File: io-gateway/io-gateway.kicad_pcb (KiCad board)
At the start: 2 copper layers, 13 parts, among them IC1 MAX17673AATI+

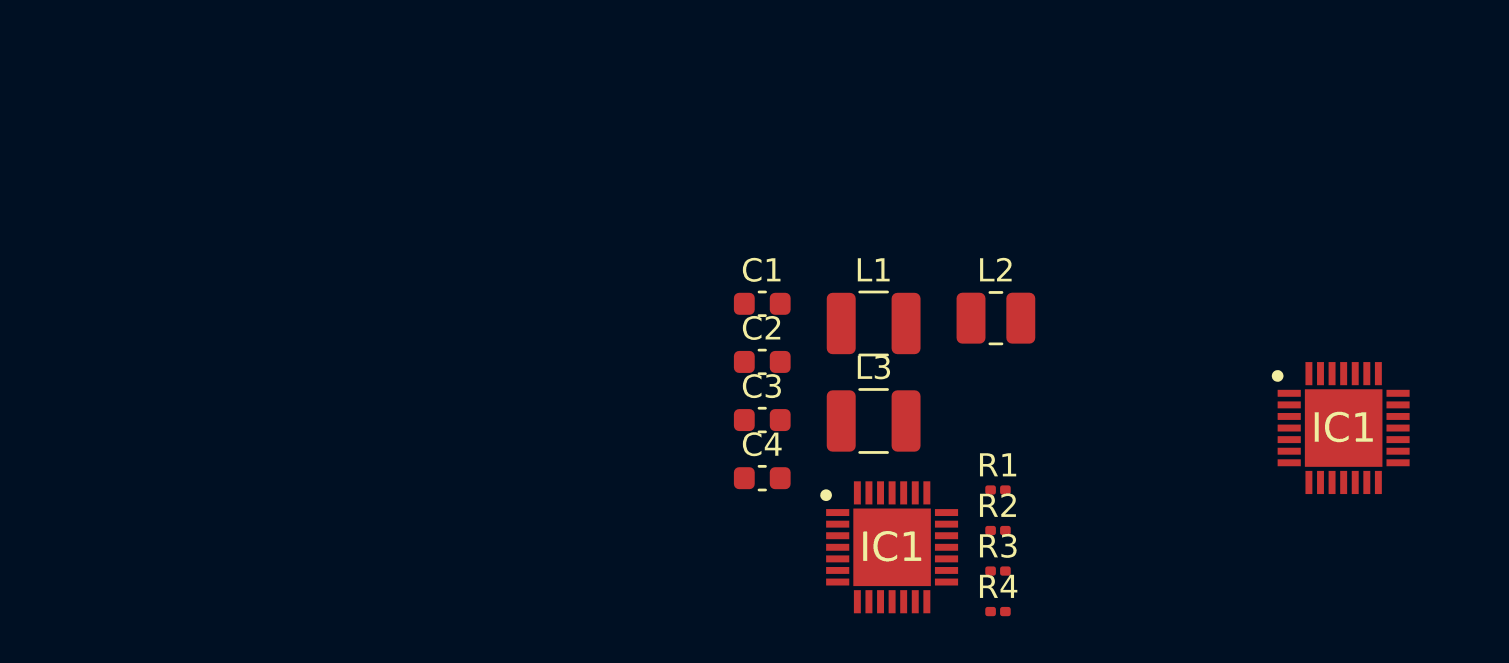
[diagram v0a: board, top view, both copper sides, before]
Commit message: buck regulator schematic ready
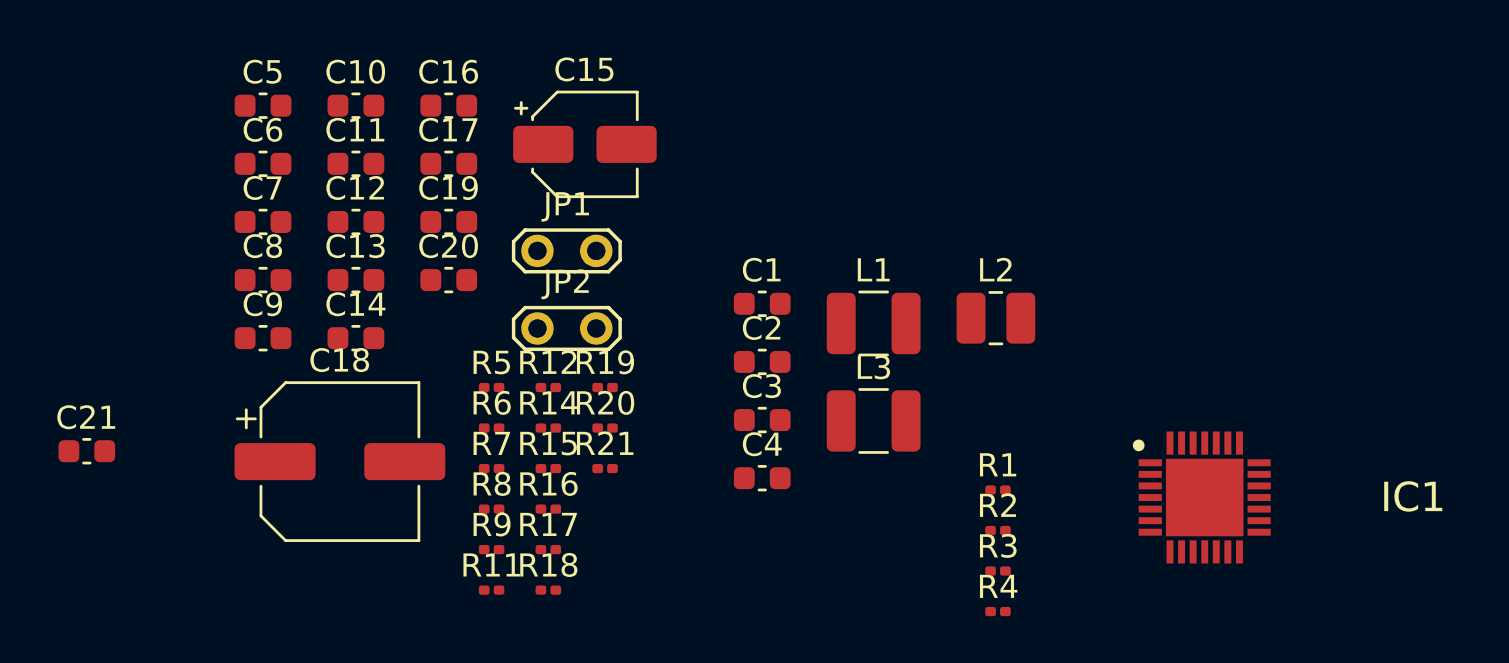
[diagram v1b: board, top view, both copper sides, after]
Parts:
- removed the IC1 at (98.5, 83.0)
- added C10: 2.2µF, Capacitor_SMD:C_0603_1608Metric, F.Cu at (55.8, 69.1)
- added C11: 47µF, Capacitor_SMD:C_0603_1608Metric, F.Cu at (55.8, 71.6)
- added C12: 1µF, Capacitor_SMD:C_0603_1608Metric, F.Cu at (55.8, 74.1)
- added C13: 2.2µF, Capacitor_SMD:C_0603_1608Metric, F.Cu at (55.8, 76.6)
- added C14: 100nF, Capacitor_SMD:C_0603_1608Metric, F.Cu at (55.8, 79.1)
- added C15: 4.7µF, Capacitor_SMD:CP_Elec_4x5.4, F.Cu at (65.7, 70.8)
- added C16: 100nF, Capacitor_SMD:C_0603_1608Metric, F.Cu at (59.9, 69.1)
- added C17: open, Capacitor_SMD:C_0603_1608Metric, F.Cu at (59.9, 71.6)
- added C18: 47µF, Capacitor_SMD:CP_Elec_6.3x5.4, F.Cu at (55.2, 84.5)
- added C19: 4.7µF, Capacitor_SMD:C_0603_1608Metric, F.Cu at (59.9, 74.1)
- added C20: 100nF, Capacitor_SMD:C_0603_1608Metric, F.Cu at (59.9, 76.6)
- added C21: 100nF, Capacitor_SMD:C_0603_1608Metric, F.Cu at (44.2, 84.0)
- added C5: 22µF, Capacitor_SMD:C_0603_1608Metric, F.Cu at (51.8, 69.1)
- added C6: open, Capacitor_SMD:C_0603_1608Metric, F.Cu at (51.8, 71.6)
- added C7: 100nF, Capacitor_SMD:C_0603_1608Metric, F.Cu at (51.8, 74.1)
- added C8: open, Capacitor_SMD:C_0603_1608Metric, F.Cu at (51.8, 76.6)
- added C9: 2.2µF, Capacitor_SMD:C_0603_1608Metric, F.Cu at (51.8, 79.1)
- added JP1: Jumper_2_Bridged, TestPoint:TestPoint_2Pads_Pitch2.54mm_Drill0.8mm, F.Cu at (63.7, 75.3)
- added JP2: Jumper_2_Bridged, TestPoint:TestPoint_2Pads_Pitch2.54mm_Drill0.8mm, F.Cu at (63.7, 78.7)
- added R11: 100R, Resistor_SMD:R_0201_0603Metric, F.Cu at (61.7, 90.0)
- added R12: 10K, Resistor_SMD:R_0201_0603Metric, F.Cu at (64.2, 81.2)
- added R14: 470K, Resistor_SMD:R_0201_0603Metric, F.Cu at (64.2, 83.0)
- added R15: 22K, Resistor_SMD:R_0201_0603Metric, F.Cu at (64.2, 84.8)
- added R16: open, Resistor_SMD:R_0201_0603Metric, F.Cu at (64.2, 86.5)
- added R17: 0R, Resistor_SMD:R_0201_0603Metric, F.Cu at (64.2, 88.2)
- added R18: open, Resistor_SMD:R_0201_0603Metric, F.Cu at (64.2, 90.0)
- added R19: open, Resistor_SMD:R_0201_0603Metric, F.Cu at (66.6, 81.2)
- added R20: open, Resistor_SMD:R_0201_0603Metric, F.Cu at (66.6, 83.0)
- added R21: 0R, Resistor_SMD:R_0201_0603Metric, F.Cu at (66.6, 84.8)
- added R5: 330k, Resistor_SMD:R_0201_0603Metric, F.Cu at (61.7, 81.2)
- added R6: 1M, Resistor_SMD:R_0201_0603Metric, F.Cu at (61.7, 83.0)
- added R7: 1R, Resistor_SMD:R_0201_0603Metric, F.Cu at (61.7, 84.8)
- added R8: 22K, Resistor_SMD:R_0201_0603Metric, F.Cu at (61.7, 86.5)
- added R9: 33K, Resistor_SMD:R_0201_0603Metric, F.Cu at (61.7, 88.2)
- C2, C3: value C -> open
- R1: value R -> 12K
- R2: value R -> 68K
- R3: value R -> 10K
- R4: value R -> 3K3
- moved IC1 13.7 mm to (92.5, 86.0)
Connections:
- IC1 pad 10: unconnected-(IC1-INA-Pad10) -> Net-(IC1-ENA)
- IC1 pad 11: unconnected-(IC1-ENA-Pad11) -> Net-(IC1-ENA)
- IC1 pad 12: unconnected-(IC1-SSH-Pad12) -> /SSH
- IC1 pad 13: unconnected-(IC1-FBH-Pad13) -> Net-(IC1-FBH)
- IC1 pad 15: unconnected-(IC1-ENH-Pad15) -> +24V
- IC1 pad 16: unconnected-(IC1-INH-Pad16) -> +24V
- IC1 pad 17: unconnected-(IC1-PGNDH-Pad17) -> GND
- IC1 pad 19: unconnected-(IC1-BSTH-Pad19) -> Net-(IC1-BSTH)
- IC1 pad 2: unconnected-(IC1-POKH-Pad2) -> Net-(IC1-POKH)
- IC1 pad 20: unconnected-(IC1-GND-Pad20) -> GND
- IC1 pad 21: unconnected-(IC1-VCC-Pad21) -> /MX_VCC
- IC1 pad 22: unconnected-(IC1-SGND-Pad22) -> GND
- IC1 pad 23: unconnected-(IC1-EXTVCC-Pad23) -> /MX_EXTVCC
- IC1 pad 24: unconnected-(IC1-FDIV-Pad24) -> Net-(IC1-FDIV)
- IC1 pad 25: unconnected-(IC1-ENB-Pad25) -> Net-(IC1-ENB)
- IC1 pad 26: unconnected-(IC1-INB-Pad26) -> Net-(IC1-ENB)
- IC1 pad 27: unconnected-(IC1-PGNDB-Pad27) -> GND
- IC1 pad 3: unconnected-(IC1-POKB-Pad3) -> Net-(IC1-POKB)
- IC1 pad 4: unconnected-(IC1-MODE/SYNC-Pad4) -> Net-(IC1-MODE/SYNC)
- IC1 pad 5: unconnected-(IC1-POKA-Pad5) -> Net-(IC1-POKA)
- IC1 pad 6: unconnected-(IC1-RT-Pad6) -> Net-(IC1-RT)
- IC1 pad 9: unconnected-(IC1-PGNDA-Pad9) -> GND
- L2 pad 2: unconnected-(L2-Pad2) -> +5V
- R1 pad 2: Net-(IC1-FBB) -> Net-(R1-Pad2)
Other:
- copper layers 2 -> 4

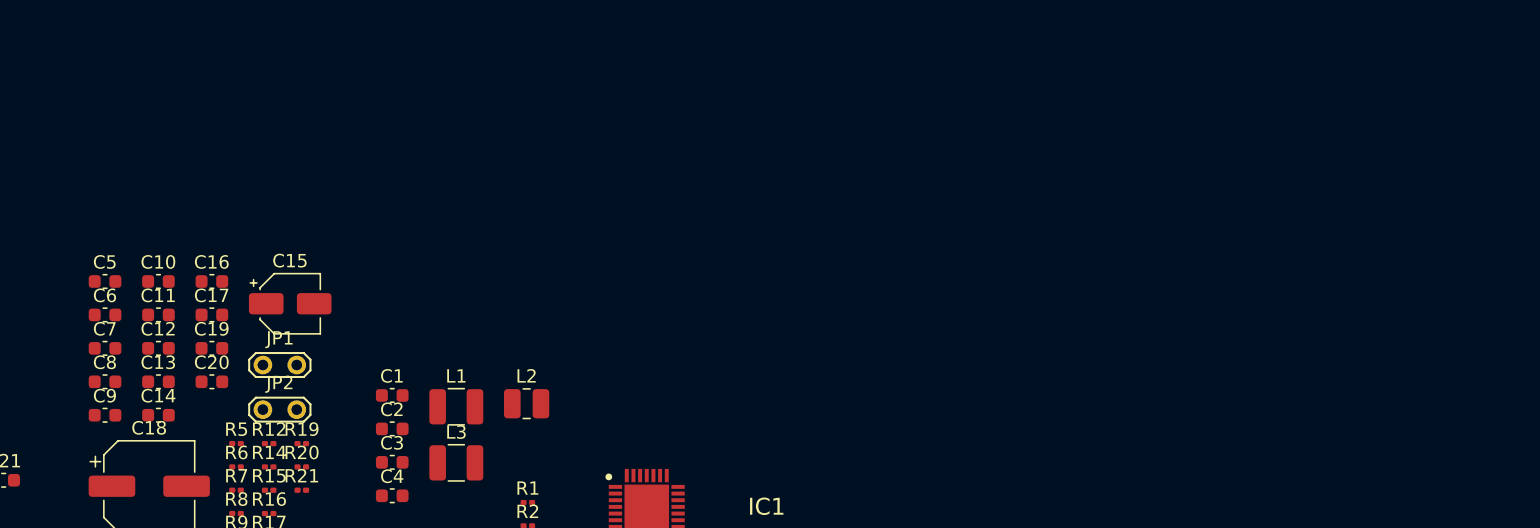
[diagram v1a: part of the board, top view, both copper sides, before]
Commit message: add some datasheets
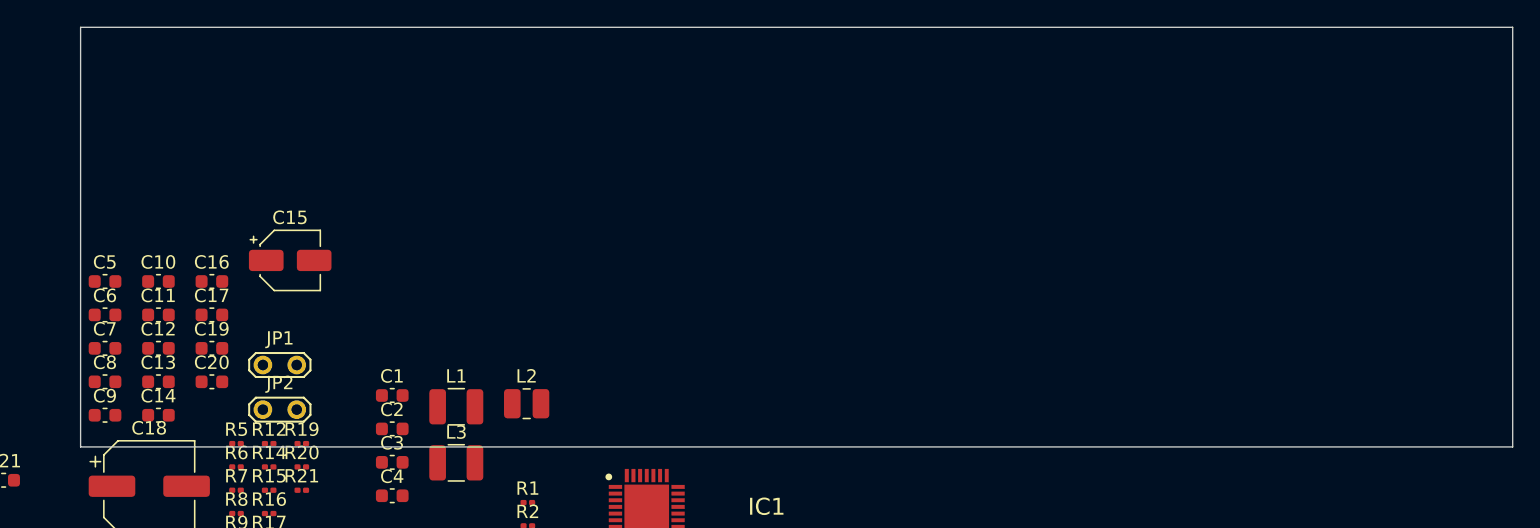
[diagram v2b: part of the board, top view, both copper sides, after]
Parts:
- moved C15 3.25 mm to (65.7, 67.5)
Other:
- board outline added: 107.5 x 31.5 mm
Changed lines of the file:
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@@
 	(footprint "Capacitor_SMD:CP_Elec_4x5.4"
 		(layer "F.Cu")
-		(at 65.735 70.75)
+		(at 65.735 67.5)
 		(descr "SMD capacitor, aluminum electrolytic, Panasonic A5 / Nichicon, 4.0x5.4mm")
 		(tags "capacitor electrolytic")
@@
 		)
 	)
+	(gr_rect
+		(start 50 50)
+		(end 157.5 81.5)
+		(stroke
+			(width 0.1)
+			(type solid)
+		)
+		(fill no)
+		(layer "Edge.Cuts")
+	)
 	(embedded_fonts no)

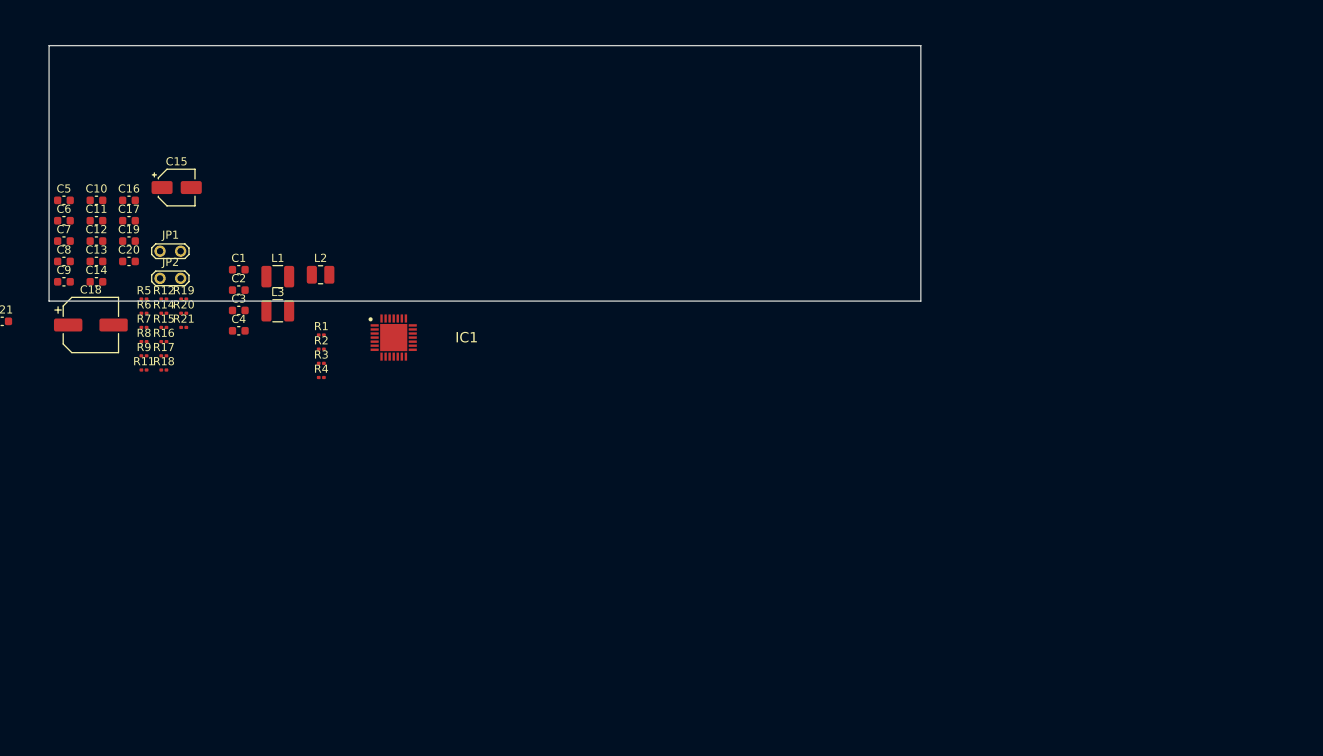
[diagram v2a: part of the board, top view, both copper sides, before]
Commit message: add Terminal Blocks
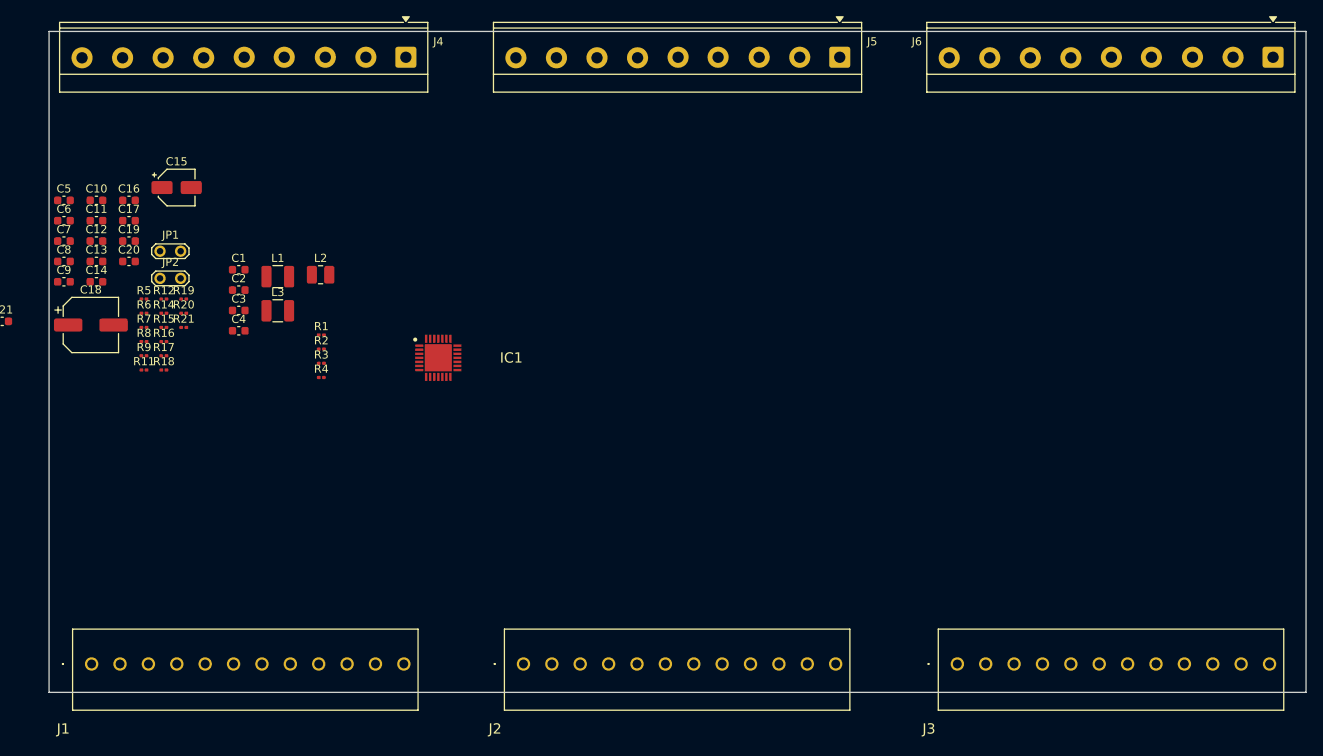
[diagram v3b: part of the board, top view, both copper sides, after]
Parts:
- added J1: 1752201, TerminalBlock_Phoenix:1752201, F.Cu at (55.2, 126.2)
- added J2: 1752201, TerminalBlock_Phoenix:1752201, F.Cu at (108.5, 126.2)
- added J3: 1752201, TerminalBlock_Phoenix:1752201, F.Cu at (162.0, 126.2)
- added J4: Screw_Terminal_01x09, TerminalBlock_TE-Connectivity:TerminalBlock_TE_282836-9_1x09_P5mm_Horizontal, F.Cu at (94.0, 51.4)
- added J5: Screw_Terminal_01x09, TerminalBlock_TE-Connectivity:TerminalBlock_TE_282836-9_1x09_P5mm_Horizontal, F.Cu at (147.5, 51.4)
- added J6: Screw_Terminal_01x09, TerminalBlock_TE-Connectivity:TerminalBlock_TE_282836-9_1x09_P5mm_Horizontal, F.Cu at (200.9, 51.4)
- moved IC1 6.04 mm to (98.0, 88.5)
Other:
- board size 107.5 x 31.5 mm -> 155 x 81.5 mm
